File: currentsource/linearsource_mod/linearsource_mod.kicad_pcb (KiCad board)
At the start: 2 copper layers, 50 x 20 mm, 17 parts, among them P1 CONN_01X04, P2 CONN_01X04, Q1 PSMN017-30BL, Q2 BC849, U1 LM358

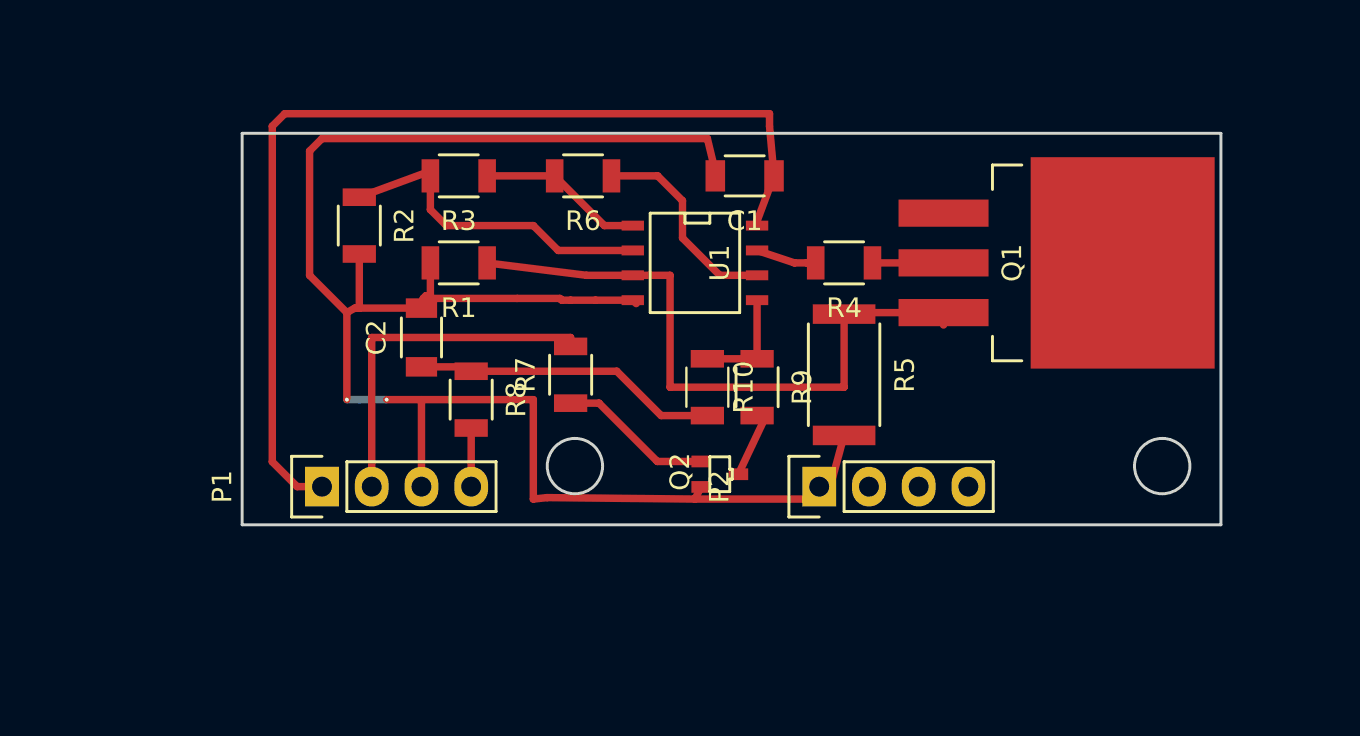
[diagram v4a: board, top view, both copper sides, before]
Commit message: currentsource: Add testpoint for Itarget
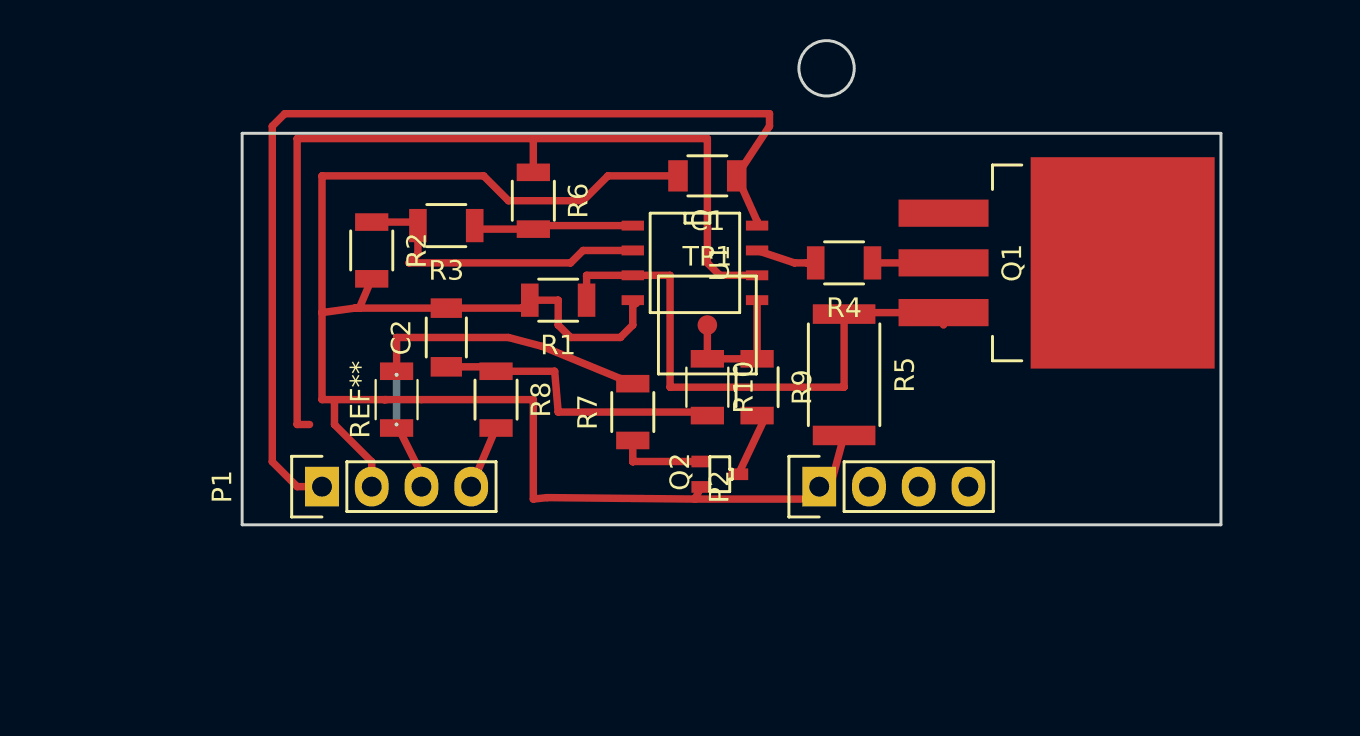
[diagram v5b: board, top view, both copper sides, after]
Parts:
- added REF**: R_1206, Resistors_SMD:R_1206, F.Cu at (154.6, 82.6)
- added TP1: TEST, SMD_Packages:1Pin, F.Cu at (170.5, 78.8)
- moved R1 5.43 mm to (162.9, 77.5)
- moved R7 3.70 mm to (166.7, 83.2)
- moved R6 2.84 mm to (161.6, 72.4), turned to 270 degrees
- moved R3 2.62 mm to (157.2, 73.7)
- moved C1 1.91 mm to (170.5, 71.2)
- moved R2 1.42 mm to (153.3, 75.0)
- moved C2 1.27 mm to (157.2, 79.4)
- moved R8 1.27 mm to (159.7, 82.6)
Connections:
- P1 pad 2: PWM -> GND
- P1 pad 3: GND -> PWM
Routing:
- net /I_feedback: track 10.7 -> 47.3 mm
- net I_sense: track 33.4 -> 29.6 mm
- net GND: track 95.6 -> 92.4 mm, vias 2 -> 0
- net Net-(Q2-Pad1): track 7.90 -> 4.93 mm
- net PWM: track 18.3 -> 20.4 mm, vias 0 -> 2
- net /I_target: track 5.53 -> 7.26 mm
- net Net-(R2-Pad1): track 16.9 -> 16.2 mm
- net VCC: track 51.8 -> 52.3 mm
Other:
- board size 50 x 20 mm -> 50 x 24.7 mm

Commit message: currentousrce: Change to edge header, incl Ifeedback
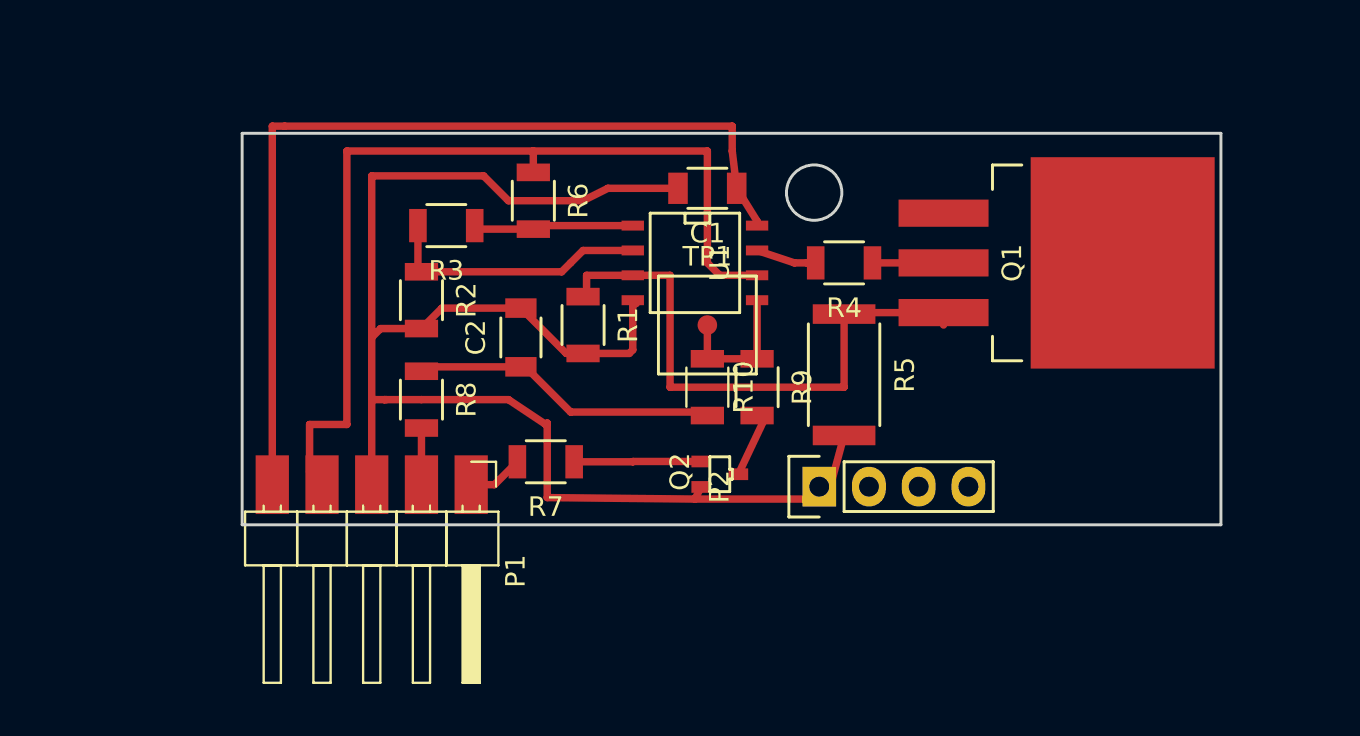
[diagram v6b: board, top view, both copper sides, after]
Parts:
- removed REF**: R_1206, Resistors_SMD:R_1206
- P1: value CONN_01X04 -> CONN_01X05; footprint Pin_Headers:Pin_Header_Straight_1x04 -> Edge:Pin_Header_Edge_1x05_Pitch2.54mm
- moved P1 7.62 mm to (158.4, 87.0), turned to 270 degrees
- moved R7 5.12 mm to (162.2, 85.8), turned to 180 degrees
- moved C2 3.81 mm to (161.0, 79.4)
- moved R8 3.81 mm to (155.9, 82.6)
- moved R2 3.59 mm to (155.9, 77.5)
- moved R1 1.80 mm to (164.1, 78.8), turned to 270 degrees
- moved C1 0.64 mm to (170.5, 71.8)
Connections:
- P1 pad 1: VCC -> PWM
- P1 pad 2: GND -> I_set
- P1 pad 3: PWM -> GND
- P1 pad 4: I_set -> I_feedback
- R6 pad 1: /I_feedback -> I_feedback
- U1 pad 6: /I_feedback -> I_feedback
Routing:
- net I_feedback: track 0.00 -> 47.5 mm
- net /I_feedback: track 47.3 -> 0.00 mm
- net PWM: track 20.4 -> 2.84 mm, vias 2 -> 0
- net GND: track 92.4 -> 82.2 mm
- net VCC: track 52.3 -> 47.3 mm
- net Net-(R2-Pad1): track 16.2 -> 13.9 mm
- net Net-(Q2-Pad1): track 4.93 -> 6.83 mm
- net Net-(C2-Pad1): track 15.4 -> 16.9 mm
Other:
- board size 50 x 24.7 mm -> 50 x 20 mm

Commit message: currentsource: Power routed, bit less wide
Fits a 50x25mm envelope including cutout with 1-2mm endmill
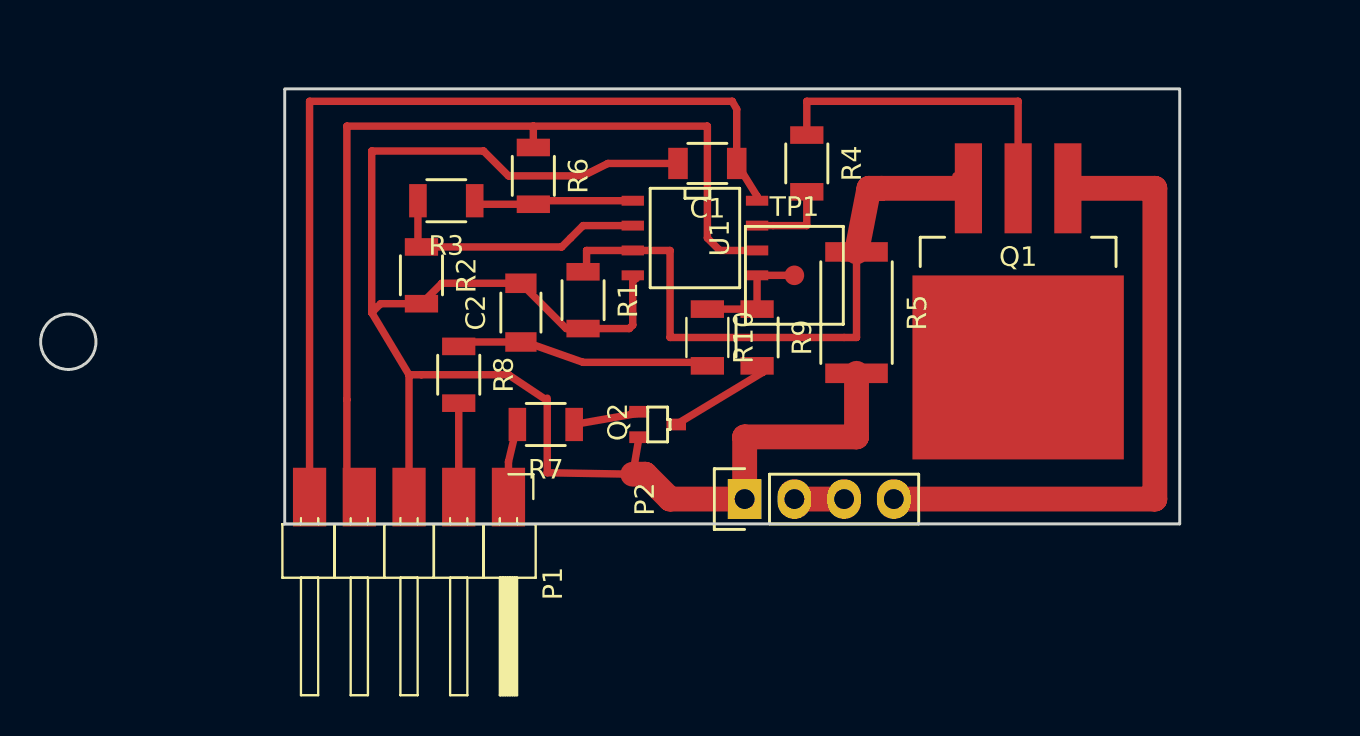
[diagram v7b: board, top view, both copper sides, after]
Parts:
- moved R4 5.43 mm to (175.6, 70.5), turned to 270 degrees
- moved Q1 5.39 mm to (186.4, 71.8), turned to 270 degrees
- moved TP1 5.12 mm to (174.9, 76.3)
- moved Q2 4.07 mm to (168.0, 83.9)
- moved P2 3.86 mm to (172.4, 87.7)
- moved R5 3.24 mm to (178.1, 78.2)
- moved R10 2.54 mm to (170.5, 79.4)
- moved R9 2.54 mm to (173.0, 79.4)
- moved R8 2.29 mm to (157.8, 81.3)
- moved P1 2.01 mm to (160.3, 87.7)
- moved R7 1.91 mm to (162.2, 83.9)
- moved C2 1.27 mm to (161.0, 78.2)
- moved R2 1.27 mm to (155.9, 76.3)
- moved R3 1.27 mm to (157.2, 72.4)
- moved U1 1.27 mm to (169.9, 74.3)
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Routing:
- net I_out-: track 0.00 -> 33.7 mm
- net Net-(Q1-Pad2): track 3.63 -> 17.0 mm
- net GND: track 82.2 -> 89.9 mm
- net I_sense: track 29.6 -> 32.9 mm
- net Net-(C2-Pad1): track 16.9 -> 14.2 mm
- net I_out+: track 0.00 -> 2.54 mm
- net Net-(Q2-Pad1): track 6.83 -> 4.37 mm
- net Net-(Q2-Pad3): track 3.41 -> 5.64 mm
- net I_set: track 2.89 -> 4.80 mm
- net Net-(R4-Pad2): track 3.10 -> 4.27 mm
- net /I_target: track 7.26 -> 6.17 mm
- net PWM: track 2.84 -> 3.76 mm
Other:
- board size 50 x 20 mm -> 58.2 x 22.2 mm
- net class Power added: clearance 0.381, trace_width 1.27, via_dia 0.2, via_drill 0.01

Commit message: currentsource: Use edge header also for power
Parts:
- P2: footprint Pin_Headers:Pin_Header_Straight_1x04 -> Edge:Pin_Header_Edge_1x04_Pitch2.54mm
- moved P2 5.72 mm to (178.1, 87.7), turned to 270 degrees
- moved Q2 1.42 mm to (166.7, 84.5)
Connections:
- P2 pad 1: GND -> I_out-
- P2 pad 4: I_out- -> GND
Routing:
- net Net-(Q2-Pad3): track 5.64 -> 9.29 mm
- net I_out-: track 33.7 -> 36.5 mm
- net I_out+: track 2.54 -> 0.00 mm
- net Net-(Q2-Pad1): track 4.37 -> 3.05 mm
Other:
- board size 58.2 x 22.2 mm -> 45.7 x 22.2 mm
